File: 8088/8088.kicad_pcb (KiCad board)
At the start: 2 copper layers, 154.9 x 93.5 mm, 142 parts, among them P10 CONN_01X15, P11 CONN_01X05, P12 CONN_01X05, P13 CONN_01X08, P14 CONN_01X08, P9 CONN_01X06, U1 8284, U10 2114, U11 ULN2803ADWR, U12 74LS14, U13 ULN2803ADWR, U14 ULN2803ADWR, U15 ULN2803ADWR, U16 LM1084IT-5.0/NOPB, U2 8088, U3 8755A, U3PA U3PA, U3PB U3PB, U4 8155, U4PA U4PA, U4PB U4PB, U4PC U4PC, U5 8251A, U6 74LS32, U7 74LS138, U8 8282, U9 2114, Y1 12MHz

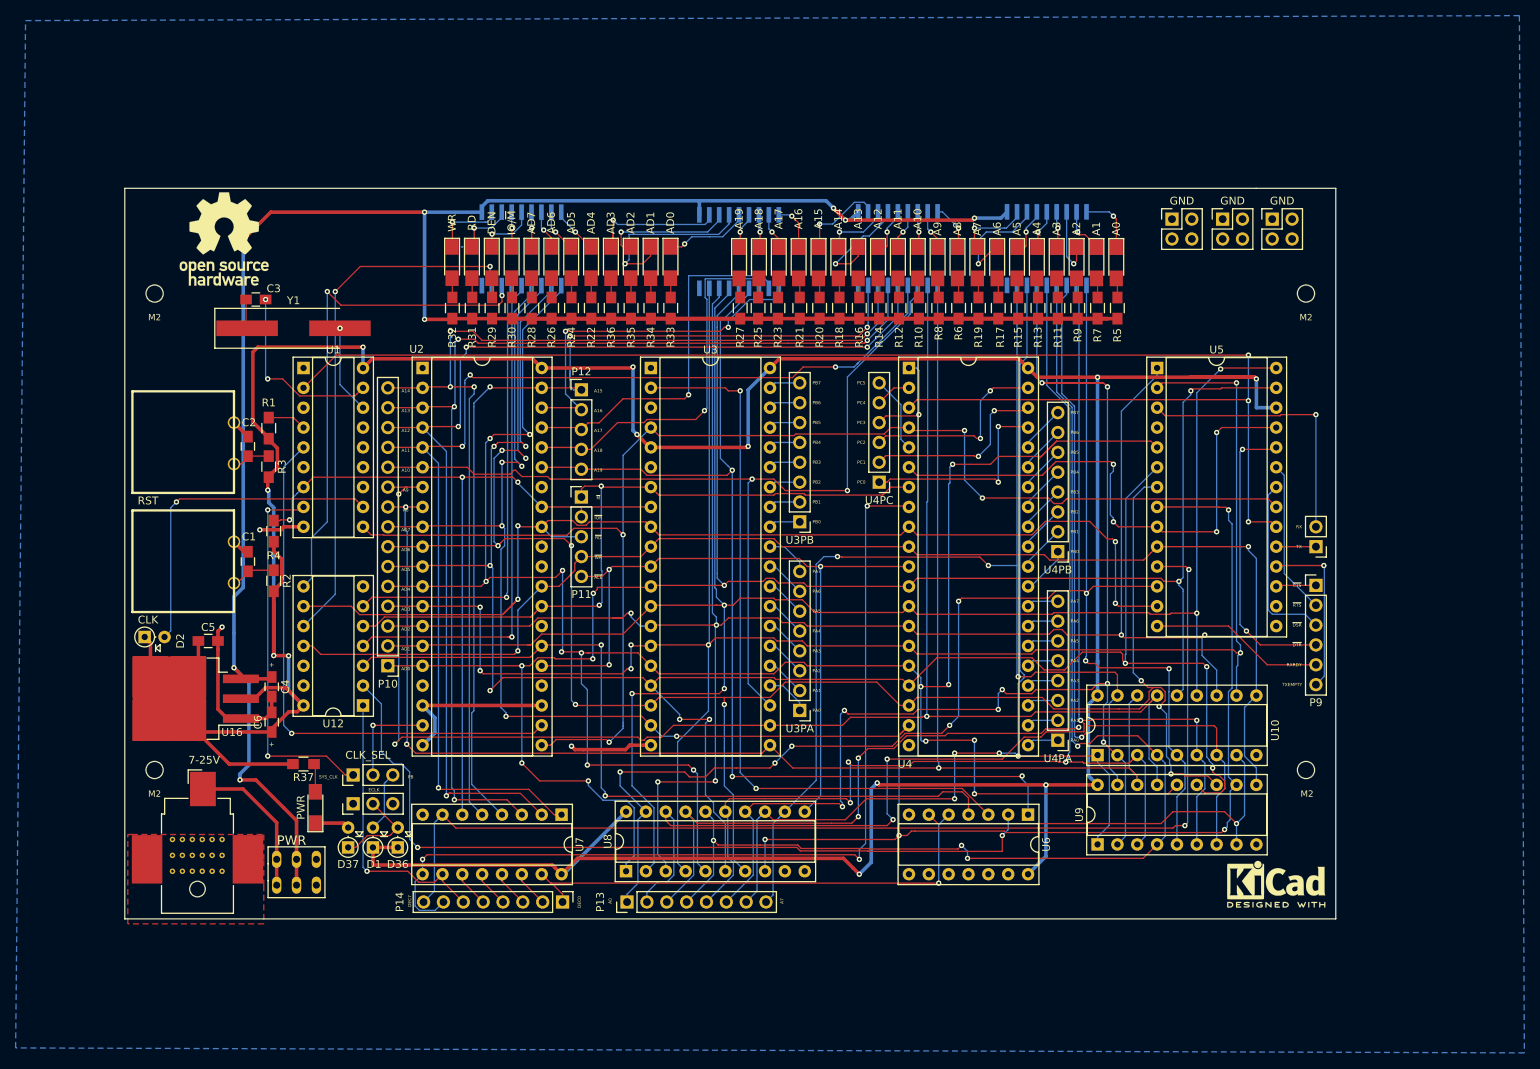
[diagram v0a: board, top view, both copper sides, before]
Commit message: Updated PCB to use top side power plane
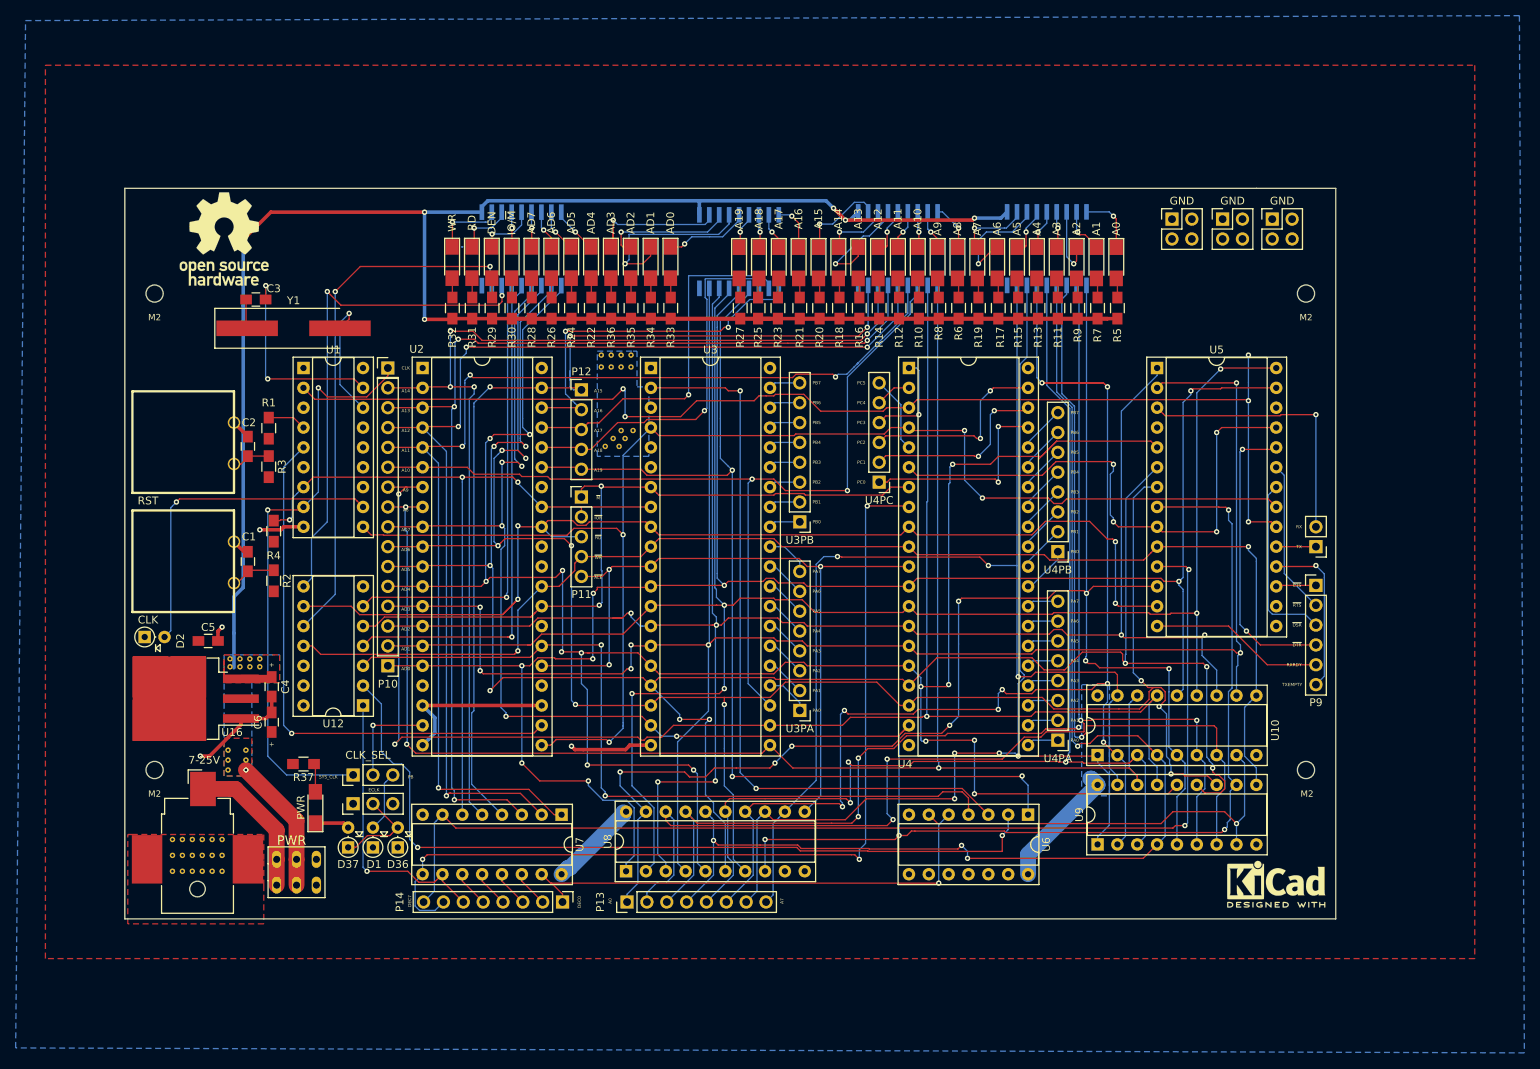
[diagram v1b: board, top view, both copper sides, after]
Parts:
- added CLK: Pin_Header_Straight_1x01_Pitch2.54mm, Pin_Headers:Pin_Header_Straight_1x01_Pitch2.54mm, F.Cu at (109.9, 64.1)
- added REF**: via-0.7mm, Library:via-0.7mm, F.Cu at (93.5, 102.4)
- added REF**: via-0.7mm, Library:via-0.7mm, F.Cu at (91.7, 113.0)
- added REF**: via-0.7mm, Library:via-0.7mm, F.Cu at (91.7, 114.3)
- added REF**: via-0.7mm, Library:via-0.7mm, F.Cu at (89.4, 114.3)
- added REF**: via-0.7mm, Library:via-0.7mm, F.Cu at (89.4, 115.6)
- added REF**: via-0.7mm, Library:via-0.7mm, F.Cu at (140.2, 73.2)
- added REF**: via-0.7mm, Library:via-0.7mm, F.Cu at (139.4, 74.2)
- added REF**: via-0.7mm, Library:via-0.7mm, F.Cu at (137.7, 74.2)
- added REF**: via-0.7mm, Library:via-0.7mm, F.Cu at (138.7, 73.2)
- added REF**: via-0.7mm, Library:via-0.7mm, F.Cu at (141.2, 72.1)
- added REF**: via-0.7mm, Library:via-0.7mm, F.Cu at (139.7, 72.1)
- added REF**: via-0.7mm, Library:via-0.7mm, F.Cu at (92.2, 102.4)
- added REF**: via-0.7mm, Library:via-0.7mm, F.Cu at (137.2, 64.0)
- added REF**: via-0.7mm, Library:via-0.7mm, F.Cu at (138.4, 64.0)
- added REF**: via-0.7mm, Library:via-0.7mm, F.Cu at (139.7, 64.0)
- added REF**: via-0.7mm, Library:via-0.7mm, F.Cu at (141.0, 64.0)
- added REF**: via-0.7mm, Library:via-0.7mm, F.Cu at (141.0, 62.5)
- added REF**: via-0.7mm, Library:via-0.7mm, F.Cu at (139.7, 62.5)
- added REF**: via-0.7mm, Library:via-0.7mm, F.Cu at (138.4, 62.5)
- added REF**: via-0.7mm, Library:via-0.7mm, F.Cu at (137.2, 62.5)
- added REF**: via-0.7mm, Library:via-0.7mm, F.Cu at (90.9, 102.4)
- added REF**: via-0.7mm, Library:via-0.7mm, F.Cu at (89.7, 102.4)
- added REF**: via-0.7mm, Library:via-0.7mm, F.Cu at (89.7, 101.3)
- added REF**: via-0.7mm, Library:via-0.7mm, F.Cu at (90.9, 101.3)
- added REF**: via-0.7mm, Library:via-0.7mm, F.Cu at (92.2, 101.3)
- added REF**: via-0.7mm, Library:via-0.7mm, F.Cu at (93.5, 101.3)
- added REF**: via-0.7mm, Library:via-0.7mm, F.Cu at (89.4, 113.0)
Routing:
- net +5V: track 472.6 -> 27.7 mm, vias 12 -> 0
- net Net-(U1-Pad2): track 191.7 -> 153.5 mm, vias 3 -> 5
- net Net-(JP1-Pad1): track 48.1 -> 75.7 mm
- net /P_IN: track 377.3 -> 359.6 mm, vias 8 -> 7
- net Net-(U1-Pad16): track 11.4 -> 16.2 mm
- net GND: track 67.7 -> 65.0 mm, vias 3 -> 4
- net Net-(C3-Pad1): track 23.8 -> 26.5 mm
- net +12V: track 19.2 -> 18.7 mm
- added copper zone on B.Cu, net +5V
- added copper zone on F.Cu, net +5V
- added copper zone on B.Cu, net /P_IN
- added copper zone on F.Cu, net /P_IN
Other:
- net class GND added: clearance 0.1524, trace_width 0.4572, via_dia 0.6858, via_drill 0.3302
- net class PWR: trace_width 0.4572 -> 2.032
- board text added: "CLK"

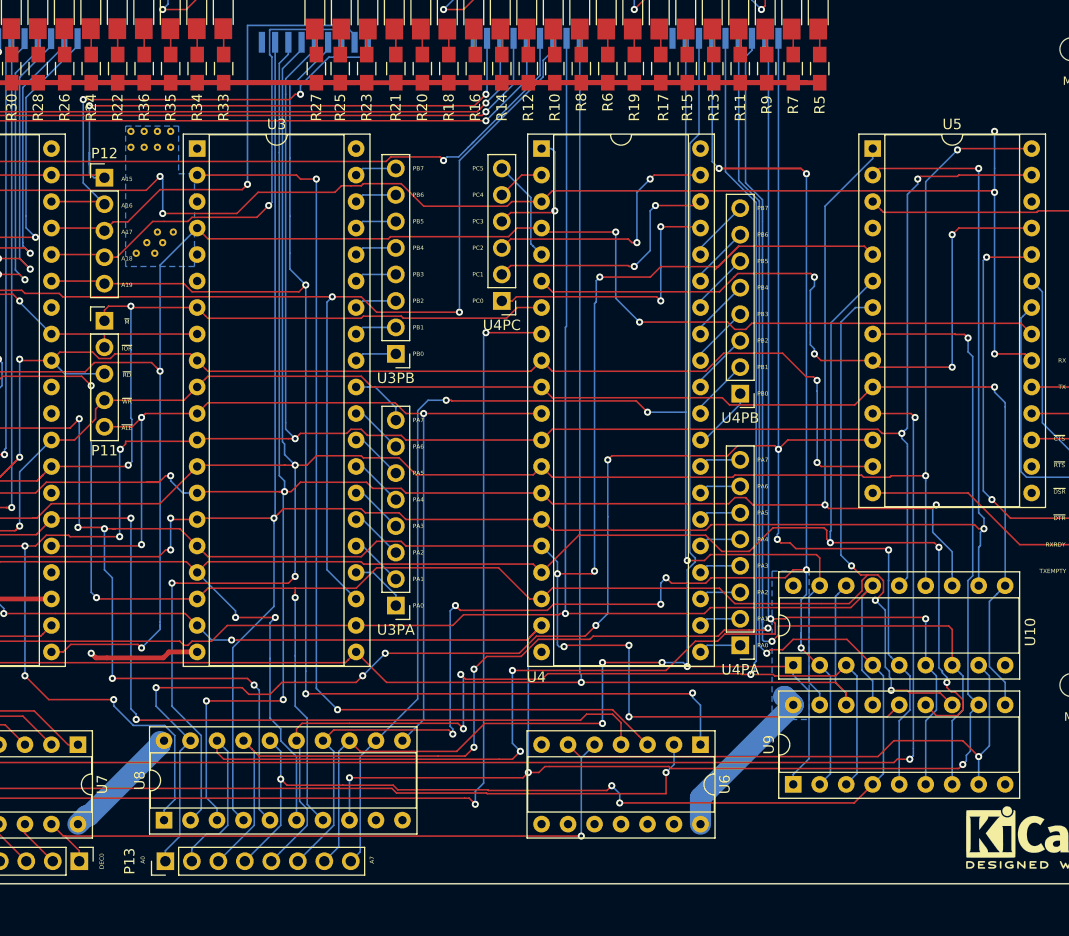
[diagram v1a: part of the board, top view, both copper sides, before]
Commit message: Fixed some track routing
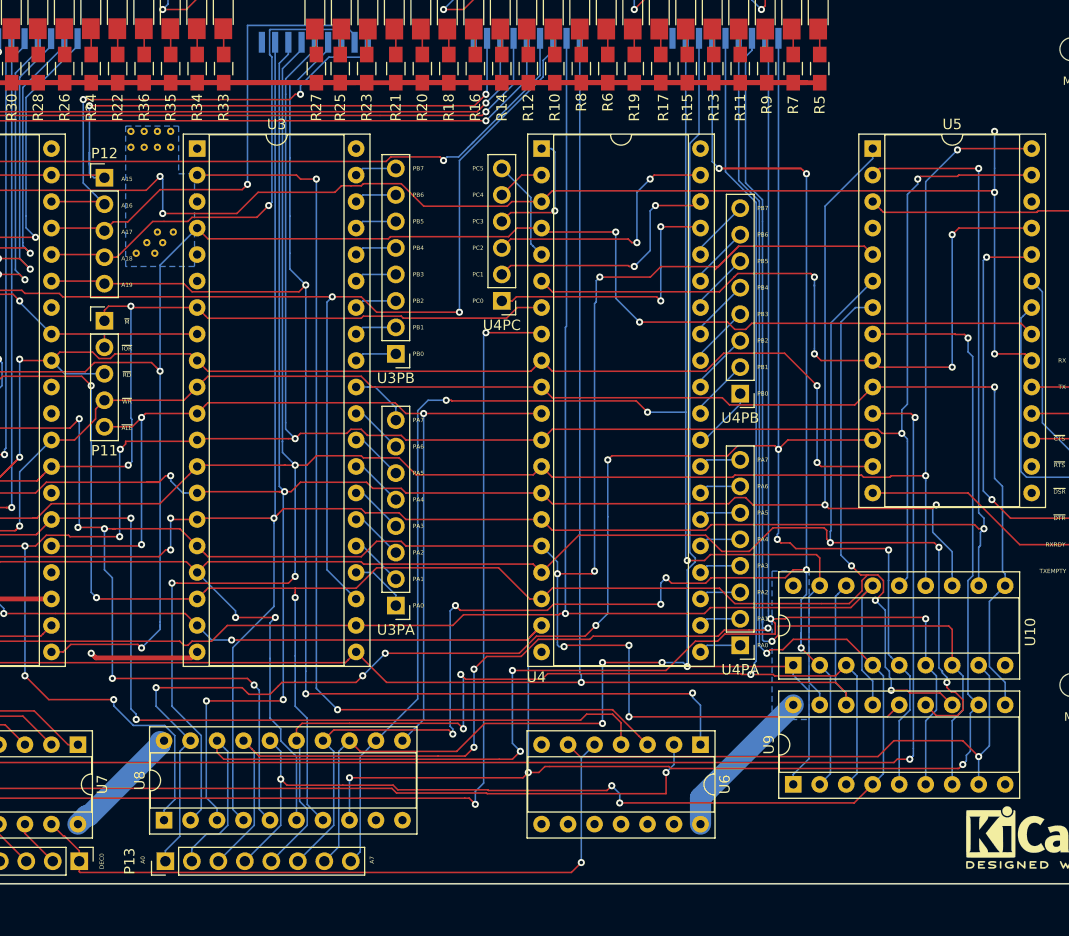
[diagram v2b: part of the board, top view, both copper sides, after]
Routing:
- net /DEC0: track 63.7 -> 66.1 mm
- net +5V: track 27.7 -> 26.4 mm

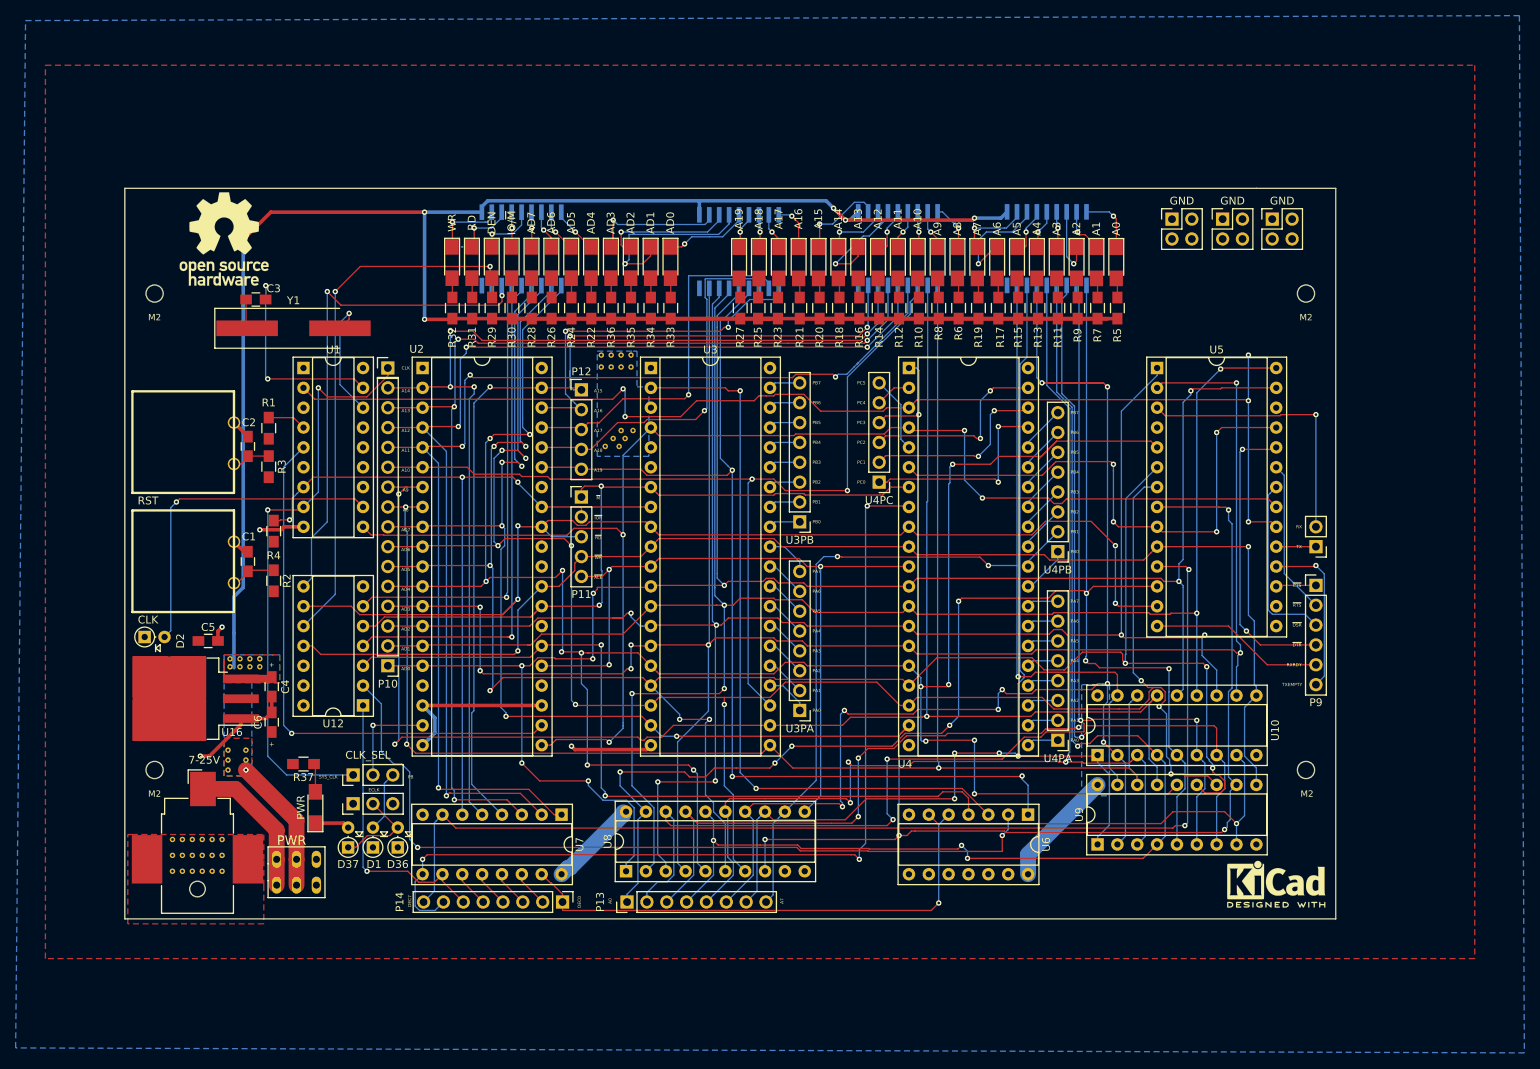
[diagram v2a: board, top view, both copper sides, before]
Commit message: Board revised based on prototype
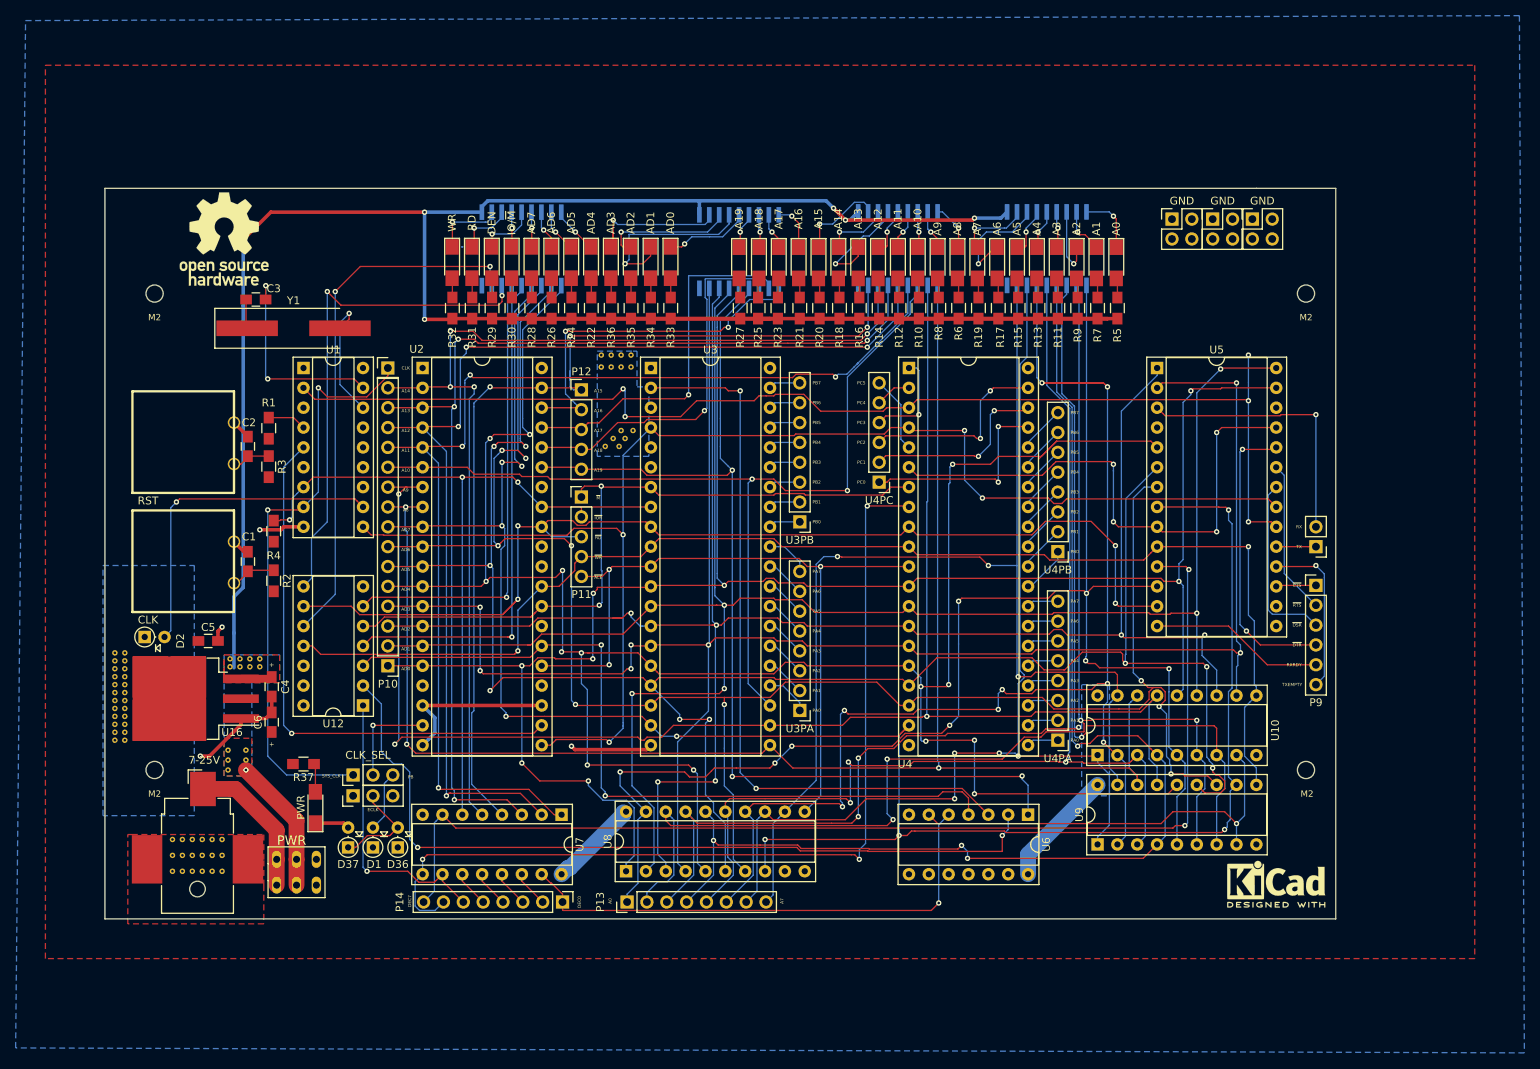
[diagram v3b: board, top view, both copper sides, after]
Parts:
- added REF**: via-0.7mm, Library:via-0.7mm, F.Cu at (76.2, 111.8)
- added REF**: via-0.7mm, Library:via-0.7mm, F.Cu at (76.2, 102.6)
- added REF**: via-0.7mm, Library:via-0.7mm, F.Cu at (76.2, 101.6)
- added REF**: via-0.7mm, Library:via-0.7mm, F.Cu at (76.2, 100.6)
- added REF**: via-0.7mm, Library:via-0.7mm, F.Cu at (74.9, 100.6)
- added REF**: via-0.7mm, Library:via-0.7mm, F.Cu at (74.9, 101.6)
- added REF**: via-0.7mm, Library:via-0.7mm, F.Cu at (74.9, 102.6)
- added REF**: via-0.7mm, Library:via-0.7mm, F.Cu at (74.9, 103.6)
- added REF**: via-0.7mm, Library:via-0.7mm, F.Cu at (74.9, 104.6)
- added REF**: via-0.7mm, Library:via-0.7mm, F.Cu at (74.9, 105.7)
- added REF**: via-0.7mm, Library:via-0.7mm, F.Cu at (74.9, 106.7)
- added REF**: via-0.7mm, Library:via-0.7mm, F.Cu at (76.2, 110.7)
- added REF**: via-0.7mm, Library:via-0.7mm, F.Cu at (74.9, 107.7)
- added REF**: via-0.7mm, Library:via-0.7mm, F.Cu at (74.9, 108.7)
- added REF**: via-0.7mm, Library:via-0.7mm, F.Cu at (74.9, 109.7)
- added REF**: via-0.7mm, Library:via-0.7mm, F.Cu at (74.9, 110.7)
- added REF**: via-0.7mm, Library:via-0.7mm, F.Cu at (74.9, 111.8)
- added REF**: via-0.7mm, Library:via-0.7mm, F.Cu at (76.2, 109.7)
- added REF**: via-0.7mm, Library:via-0.7mm, F.Cu at (76.2, 108.7)
- added REF**: via-0.7mm, Library:via-0.7mm, F.Cu at (76.2, 107.7)
- added REF**: via-0.7mm, Library:via-0.7mm, F.Cu at (76.2, 106.7)
- added REF**: via-0.7mm, Library:via-0.7mm, F.Cu at (76.2, 105.7)
- added REF**: via-0.7mm, Library:via-0.7mm, F.Cu at (76.2, 104.6)
- added REF**: via-0.7mm, Library:via-0.7mm, F.Cu at (76.2, 103.6)
- moved GND 2.54 mm to (220.5, 45.1)
- moved GND 1.27 mm to (215.4, 45.1)
- moved JP2 1.02 mm to (105.4, 118.9)
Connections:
- JP2 pad 1: Net-(JP2-Pad1) -> GND
- JP2 pad 3: Net-(JP2-Pad3) -> GND
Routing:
- net /ECLK: track 11.8 -> 12.9 mm
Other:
- board size 154.9 x 93.5 mm -> 157.5 x 93.5 mm
